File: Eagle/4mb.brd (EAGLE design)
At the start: 222 x 40 mm, 28 parts

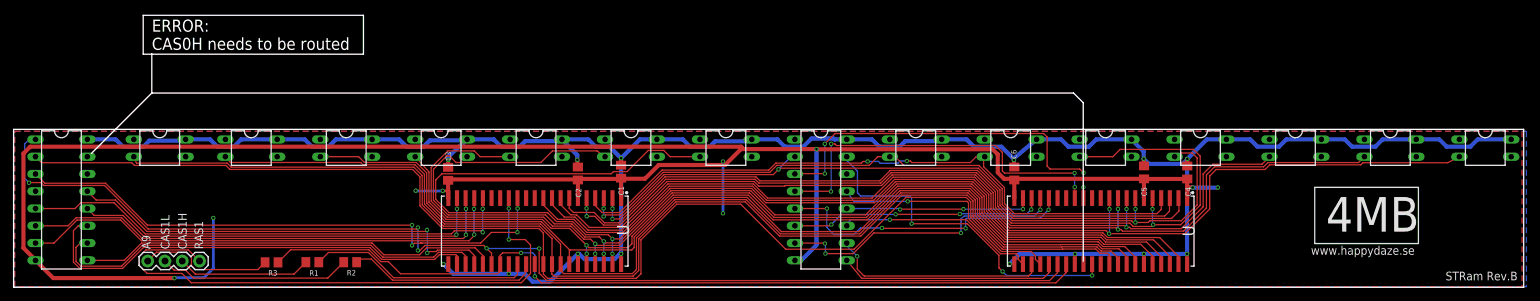
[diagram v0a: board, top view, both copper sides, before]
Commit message: Routed CAS0H
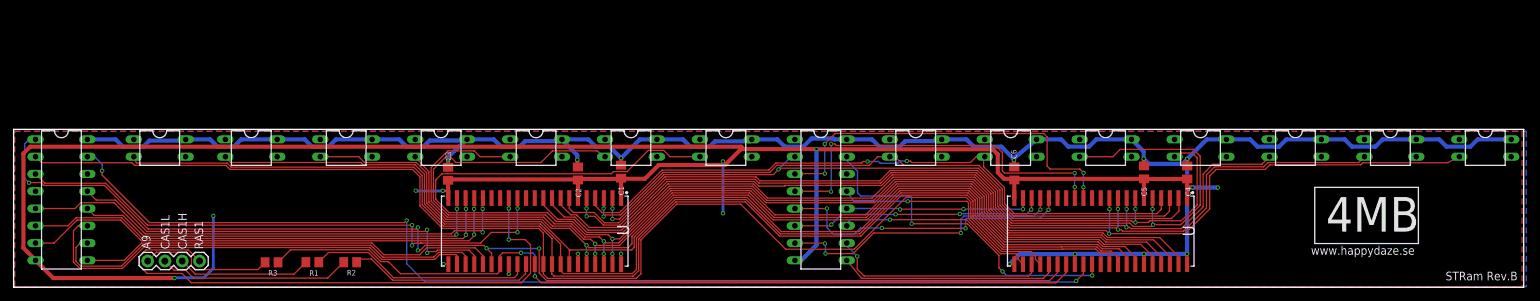
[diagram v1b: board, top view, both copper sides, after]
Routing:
- net CAS0H: track 0.00 -> 160.9 mm, vias 0 -> 3
- net GND: track 337.8 -> 294.2 mm
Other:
- board size 222 x 40 mm -> 222 x 23.2 mm
- board text removed: "ERROR: CAS0H needs to be routed"
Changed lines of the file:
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@@
 <?xml version="1.0" encoding="utf-8"?>
 <!DOCTYPE eagle SYSTEM "eagle.dtd">
-<eagle version="9.4.2">
+<eagle version="9.6.2">
 <drawing>
 <settings>
-<setting alwaysvectorfont="no"/>
+<setting alwaysvectorfont="yes"/>
 <setting verticaltext="up"/>
 </settings>
-<grid distance="25" unitdist="mil" unit="mil" style="lines" multiple="1" display="no" altdistance="1" altunitdist="mil" altunit="mil"/>
+<grid distance="12.5" unitdist="mil" unit="mil" style="lines" multiple="1" display="no" altdistance="1" altunitdist="mil" altunit="mil"/>
 <layers>
 <layer number="1" name="Top" color="4" fill="1" visible="yes" active="yes"/>
@@
 <wire x1="206.5274" y1="14.7066" x2="206.5274" y2="6.4516" width="0.1778" layer="25"/>
 <wire x1="206.5274" y1="6.4516" x2="191.2874" y2="6.4516" width="0.1778" layer="25"/>
-<text x="20.32" y="34.925" size="1.778" layer="20">ERROR:
-CAS0H needs to be routed</text>
-<wire x1="20.32" y1="34.29" x2="20.32" y2="28.575" width="0.1524" layer="20"/>
-<wire x1="20.32" y1="28.575" x2="11.43" y2="19.685" width="0.1524" layer="20"/>
-<wire x1="20.32" y1="28.575" x2="155.829" y2="28.575" width="0.1524" layer="20"/>
-<wire x1="155.829" y1="28.575" x2="157.2514" y2="27.1526" width="0.1524" layer="20"/>
-<wire x1="157.2514" y1="27.1526" x2="157.2514" y2="3.8608" width="0.1524" layer="20"/>
-<wire x1="20.32" y1="34.29" x2="19.05" y2="34.29" width="0.1524" layer="20"/>
-<wire x1="19.05" y1="34.29" x2="19.05" y2="40.005" width="0.1524" layer="20"/>
-<wire x1="19.05" y1="40.005" x2="51.435" y2="40.005" width="0.1524" layer="20"/>
-<wire x1="51.435" y1="40.005" x2="51.435" y2="34.29" width="0.1524" layer="20"/>
-<wire x1="51.435" y1="34.29" x2="20.32" y2="34.29" width="0.1524" layer="20"/>
 </plain>
 <attributes>
@@
 <wire x1="119.5606" y1="11.59071875" x2="119.567740625" y2="11.597859375" width="0.1778" layer="16"/>
 <wire x1="119.567740625" y1="11.597859375" x2="114.8624" y2="11.597859375" width="0.1778" layer="1"/>
-<wire x1="68.995028125" y1="11.586259375" x2="114.8624" y2="11.597859375" width="0" layer="19" extent="1-1"/>
+<wire x1="68.995028125" y1="13.1349" x2="114.8624" y2="11.597859375" width="0" layer="19" extent="1-1"/>
 </signal>
 <signal name="A1">
@@
 <wire x1="119.3673" y1="4.9657" x2="119.3546" y2="4.9784" width="0.1778" layer="1"/>
 <wire x1="123.42311875" y1="4.9657" x2="119.3673" y2="4.9657" width="0.1778" layer="1"/>
-<wire x1="67.7164" y1="7.7625" x2="114.8624" y2="6.517859375" width="0" layer="19" extent="16-16"/>
+<wire x1="67.7164" y1="7.7625" x2="114.8624" y2="6.517859375" width="0" layer="19" extent="1-1"/>
 </signal>
 <signal name="A2">
@@
 <wire x1="148.9964" y1="10.8458" x2="139.1608" y2="10.8458" width="0.1778" layer="16"/>
 <wire x1="139.1002" y1="10.7852" x2="139.1608" y2="10.8458" width="0.1778" layer="16"/>
-<wire x1="66.4972" y1="7.7371" x2="114.8624" y2="9.057859375" width="0" layer="19" extent="16-16"/>
+<wire x1="66.4972" y1="7.7371" x2="114.8624" y2="9.057859375" width="0" layer="19" extent="1-1"/>
 </signal>
 <signal name="A3">
@@
 <wire x1="122.94056875" y1="9.9568" x2="122.4824" y2="9.057859375" width="0.1778" layer="16"/>
 <wire x1="128.8288" y1="9.9568" x2="140.092625" y2="9.9568" width="0.1778" layer="1"/>
-<wire x1="65.185028125" y1="4.639571875" x2="122.4824" y2="9.057859375" width="0" layer="19" extent="1-1"/>
+<wire x1="65.185028125" y1="3.4259" x2="122.4824" y2="9.057859375" width="0" layer="19" extent="1-1"/>
 </signal>
 <signal name="A5">
@@
 <wire x1="124.0282" y1="4.572" x2="122.082340625" y2="6.517859375" width="0.1778" layer="16"/>
 <wire x1="122.082340625" y1="6.517859375" x2="122.4824" y2="6.517859375" width="0.1778" layer="16"/>
-<wire x1="66.455028125" y1="4.614171875" x2="122.082340625" y2="6.517859375" width="0" layer="19" extent="1-16"/>
+<wire x1="66.455028125" y1="3.4259" x2="122.4824" y2="6.517859375" width="0" layer="19" extent="1-1"/>
 </signal>
 <signal name="A6">
@@
 <wire x1="131.445" y1="12.6492" x2="123.5302875" y2="12.6492" width="0.1778" layer="16"/>
 <wire x1="123.5302875" y1="12.6492" x2="122.4824" y2="14.137859375" width="0.1778" layer="16"/>
-<wire x1="67.750428125" y1="4.690371875" x2="122.4824" y2="14.137859375" width="0" layer="19" extent="1-1"/>
+<wire x1="67.725028125" y1="3.4259" x2="122.4824" y2="14.137859375" width="0" layer="19" extent="1-1"/>
 </signal>
 <signal name="A7">
@@
 <wire x1="151.384" y1="1.3335" x2="124.6859875" y2="1.3335" width="0.1778" layer="1"/>
 <wire x1="124.6859875" y1="1.3335" x2="122.4824" y2="3.977859375" width="0.1778" layer="1"/>
-<wire x1="69.020428125" y1="3.4513" x2="122.4824" y2="3.977859375" width="0" layer="19" extent="1-1"/>
+<wire x1="68.995028125" y1="3.4259" x2="122.4824" y2="3.977859375" width="0" layer="19" extent="1-1"/>
 </signal>
 <signal name="A8">
@@
 <wire x1="29.3624" y1="2.8194" x2="27.9908" y2="1.4478" width="0.4064" layer="16"/>
 <wire x1="27.9908" y1="1.4478" x2="27.9908" y2="1.4224" width="0.4064" layer="16"/>
-<wire x1="29.3624" y1="2.8194" x2="29.3624" y2="10.2108" width="0.4064" layer="16"/>
+<wire x1="29.3624" y1="2.8194" x2="29.3624" y2="10.5283" width="0.4064" layer="16"/>
 <via x="63.0936" y="14.1986" extent="1-16" drill="0.35"/>
 <via x="59.1058" y="14.224" extent="1-16" drill="0.35"/>
@@
 <wire x1="5.8278875" y1="1.3716" x2="3.221628125" y2="3.977859375" width="0.6096" layer="1"/>
 <wire x1="5.8278875" y1="1.3716" x2="23.6474" y2="1.3716" width="0.6096" layer="1"/>
-<via x="29.3624" y="10.2108" extent="1-16" drill="0.35"/>
+<via x="29.3624" y="10.5283" extent="1-16" drill="0.35"/>
 </signal>
 <signal name="RAS0">
@@
 <contactref element="U$1" pad="30"/>
 <contactref element="U$3" pad="15"/>
-<wire x1="10.841628125" y1="19.217859375" x2="157.284628125" y2="3.4259" width="0" layer="19" extent="1-1"/>
+<wire x1="157.284628125" y1="3.4259" x2="157.284628125" y2="2.027128125" width="0.1778" layer="1"/>
+<wire x1="157.284628125" y1="2.027128125" x2="156.21" y2="0.9525" width="0.1778" layer="1"/>
+<via x="156.21" y="0.9525" extent="1-16" drill="0.35"/>
+<wire x1="156.21" y1="0.9525" x2="156.0604" y2="0.8029" width="0.1778" layer="16"/>
+<wire x1="156.0604" y1="0.8029" x2="60.4746" y2="0.8029" width="0.1778" layer="16"/>
+<wire x1="60.4746" y1="0.8029" x2="57.785" y2="3.4925" width="0.1778" layer="16"/>
+<wire x1="57.785" y1="3.4925" x2="57.785" y2="9.8425" width="0.1778" layer="16"/>
+<via x="57.785" y="9.8425" extent="1-16" drill="0.35"/>
+<wire x1="57.785" y1="9.8425" x2="57.4675" y2="9.525" width="0.1778" layer="1"/>
+<wire x1="57.4675" y1="9.525" x2="20.0025" y2="9.525" width="0.1778" layer="1"/>
+<wire x1="13.0175" y1="16.51" x2="13.0175" y2="17.145" width="0.1778" layer="1"/>
+<via x="13.0175" y="17.145" extent="1-16" drill="0.35"/>
+<wire x1="13.0175" y1="17.145" x2="13.0175" y2="18.0975" width="0.1778" layer="16"/>
+<wire x1="11.897140625" y1="19.217859375" x2="10.841628125" y2="19.217859375" width="0.1778" layer="16"/>
+<wire x1="20.0025" y1="9.525" x2="13.0175" y2="16.51" width="0.1778" layer="1"/>
+<wire x1="13.0175" y1="18.0975" x2="11.897140625" y2="19.217859375" width="0.1778" layer="16"/>
 </signal>
 <signal name="CAS0L">
@@
 <wire x1="157.2768" y1="14.732" x2="157.2768" y2="16.8148" width="0.1778" layer="16"/>
 <wire x1="157.2768" y1="16.8148" x2="157.3022" y2="16.8402" width="0.1778" layer="16"/>
-<wire x1="74.075028125" y1="13.1349" x2="114.472428125" y2="16.728659375" width="0" layer="19" extent="1-1"/>
+<wire x1="74.075028125" y1="13.1349" x2="114.8624" y2="16.677859375" width="0" layer="19" extent="1-1"/>
 </signal>
 <signal name="RAS1">
@@
 <wire x1="156.0322" y1="4.9022" x2="147.9042" y2="4.9022" width="0.6096" layer="16"/>
 <wire x1="147.9042" y1="4.9022" x2="146.431" y2="3.429" width="0.6096" layer="16"/>
-<wire x1="89.3064" y1="4.9431" x2="89.3064" y2="18.9992" width="0.6096" layer="16"/>
-<wire x1="89.3064" y1="4.9431" x2="89.14599375" y2="4.9431" width="0.6096" layer="16"/>
-<wire x1="83.14220625" y1="4.9431" x2="82.9564" y2="4.9431" width="0.6096" layer="16"/>
-<wire x1="89.14599375" y1="4.9431" x2="88.36139375" y2="4.1585" width="0.6096" layer="16"/>
-<wire x1="88.36139375" y1="4.1585" x2="83.92680625" y2="4.1585" width="0.6096" layer="16"/>
-<wire x1="83.92680625" y1="4.1585" x2="83.14220625" y2="4.9431" width="0.6096" layer="16"/>
-<wire x1="75.15670625" y1="1.9911" x2="72.7964" y2="1.9911" width="0.6096" layer="16"/>
-<wire x1="76.30680625" y1="0.841" x2="75.15670625" y2="1.9911" width="0.6096" layer="16"/>
-<wire x1="78.8543" y1="0.841" x2="76.30680625" y2="0.841" width="0.6096" layer="16"/>
-<wire x1="82.9564" y1="4.9431" x2="78.8543" y2="0.841" width="0.6096" layer="16"/>
-<wire x1="72.7964" y1="1.9911" x2="64.6331" y2="1.9911" width="0.6096" layer="16"/>
-<wire x1="64.6331" y1="1.9911" x2="63.1952" y2="3.429" width="0.6096" layer="16"/>
 </signal>
 <signal name="N$2">
@@
 </drawing>
 <compatibility>
-<note version="6.3" minversion="6.2.2" severity="warning">
-Since Version 6.2.2 text objects can contain more than one line,
-which will not be processed correctly with this version.
-</note>
 <note version="8.2" severity="warning">
 Since Version 8.2, EAGLE supports online libraries. The ids

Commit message: Board rev.C
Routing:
- net +5V: track 324.6 -> 48.1 mm
- net GND: track 294.2 -> 17.7 mm
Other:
- board text added: "STRam Rev.C"
- board text removed: "STRam Rev.B"
